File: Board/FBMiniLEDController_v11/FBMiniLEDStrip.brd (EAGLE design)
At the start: 17.8 x 82.5 mm, 20 parts, among them J4 POWER_JACKPTH_LOCK, U1 74LVC2T45

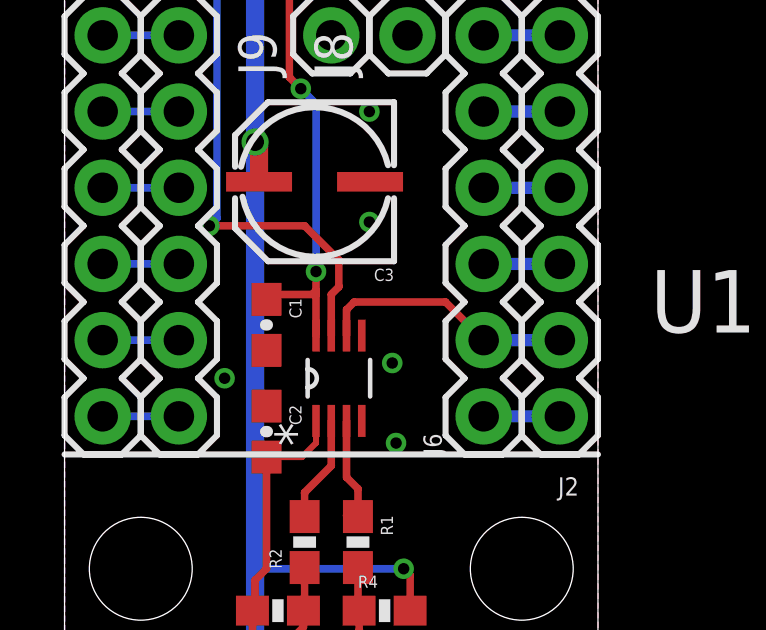
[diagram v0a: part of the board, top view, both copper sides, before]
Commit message: Updated v1.1 schematic with a lot more good information - no board changes.
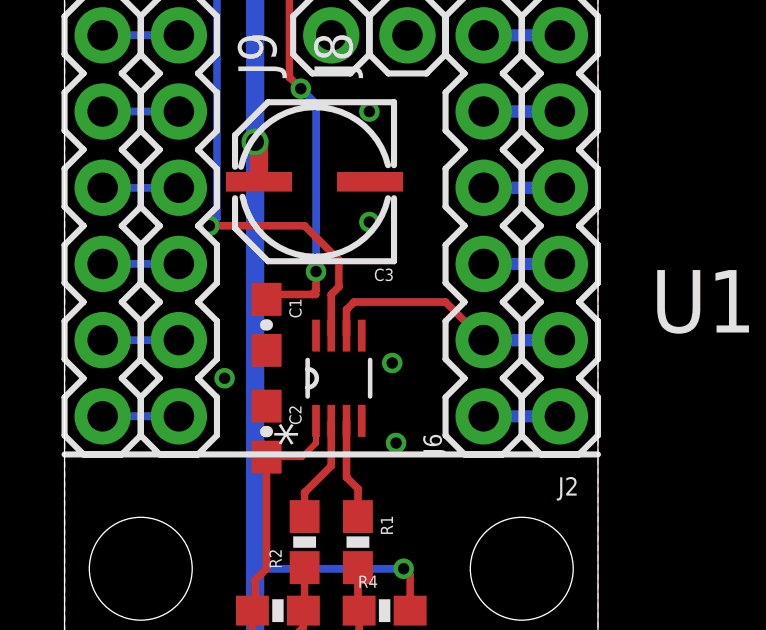
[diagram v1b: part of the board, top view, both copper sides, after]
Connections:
- net N$10 renamed 4
- net N$11 renamed 5
- net N$12 renamed 6
- net N$13 renamed 7
- net N$14 renamed 8
- net N$15 renamed 9
- net N$16 renamed 10
- net N$17 renamed 11
- net N$18 renamed 12
- net N$19 renamed 13
- net N$20 renamed 14
- net N$21 renamed 15
- net N$22 renamed 16
- net N$26 renamed N.C
- net N$27 renamed 32
- net N$28 renamed 31
- net N$29 renamed 30
- net N$30 renamed 29
- net N$31 renamed 28
- net N$32 renamed 27
- net N$33 renamed 26
- net N$34 renamed 25
- net N$35 renamed 24
- net N$36 renamed 23
- net N$37 renamed 22
- net N$38 renamed 21
- net N$39 renamed 20
- net N$40 renamed 19
- net N$41 renamed 18
- net N$42 renamed 17
- net N$9 renamed 3
- removed net N$25: C1.1, J2.18, J6.18, U1.8
- new net +3.3V: C1.1, J2.18, J6.18
- new net +3V3: U1.8
- new net 0: J1.4
- new net 1: J1.5
- new net 2: J1.6
- new net 3.3V_: J1.3
- new net VOUT: J1.1
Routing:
- net N$25: track 49.8 -> 0.00 mm, vias 2 -> 0
- net +3.3V: track 0.00 -> 48.5 mm, vias 0 -> 2
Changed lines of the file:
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@@
 </elements>
 <signals>
-<signal name="N$9">
+<signal name="3">
 <contactref element="J1" pad="7"/>
 <contactref element="J5" pad="1"/>
@@
 <wire x1="8.89" y1="29.464" x2="8.89" y2="28.0924" width="0.254" layer="1"/>
 </signal>
-<signal name="N$10">
+<signal name="4">
 <contactref element="J1" pad="8"/>
 <contactref element="J5" pad="2"/>
 <wire x1="3.81" y1="55.88" x2="1.27" y2="55.88" width="0.254" layer="16"/>
 </signal>
-<signal name="N$11">
+<signal name="5">
 <contactref element="J1" pad="9"/>
 <contactref element="J5" pad="3"/>
 <wire x1="1.27" y1="53.34" x2="3.81" y2="53.34" width="0.254" layer="16"/>
 </signal>
-<signal name="N$12">
+<signal name="6">
 <contactref element="J1" pad="10"/>
 <contactref element="J5" pad="4"/>
 <wire x1="3.81" y1="50.8" x2="1.27" y2="50.8" width="0.254" layer="16"/>
 </signal>
-<signal name="N$13">
+<signal name="7">
 <contactref element="J1" pad="11"/>
 <contactref element="J5" pad="5"/>
 <wire x1="1.27" y1="48.26" x2="3.81" y2="48.26" width="0.254" layer="16"/>
 </signal>
-<signal name="N$14">
+<signal name="8">
 <contactref element="J1" pad="12"/>
 <contactref element="J5" pad="6"/>
 <wire x1="3.81" y1="45.72" x2="1.27" y2="45.72" width="0.254" layer="16"/>
 </signal>
-<signal name="N$15">
+<signal name="9">
 <contactref element="J1" pad="13"/>
 <contactref element="J5" pad="7"/>
 <wire x1="3.81" y1="43.18" x2="1.27" y2="43.18" width="0.254" layer="16"/>
 </signal>
-<signal name="N$16">
+<signal name="10">
 <contactref element="J1" pad="14"/>
 <contactref element="J5" pad="8"/>
 <wire x1="1.27" y1="40.64" x2="3.81" y2="40.64" width="0.254" layer="16"/>
 </signal>
-<signal name="N$17">
+<signal name="11">
 <contactref element="J1" pad="15"/>
 <contactref element="J5" pad="9"/>
 <wire x1="3.81" y1="38.1" x2="1.27" y2="38.1" width="0.254" layer="16"/>
 </signal>
-<signal name="N$18">
+<signal name="12">
 <contactref element="J1" pad="16"/>
 <contactref element="J5" pad="10"/>
 <wire x1="3.81" y1="35.56" x2="1.27" y2="35.56" width="0.254" layer="16"/>
 </signal>
-<signal name="N$19">
+<signal name="13">
 <contactref element="J1" pad="17"/>
 <contactref element="J5" pad="11"/>
 <wire x1="1.27" y1="33.02" x2="3.81" y2="33.02" width="0.254" layer="16"/>
 </signal>
-<signal name="N$20">
+<signal name="14">
 <contactref element="J1" pad="18"/>
 <contactref element="J5" pad="12"/>
 <wire x1="3.81" y1="30.48" x2="1.27" y2="30.48" width="0.254" layer="16"/>
 </signal>
-<signal name="N$21">
+<signal name="15">
 <contactref element="J1" pad="19"/>
 <contactref element="J5" pad="13"/>
 <wire x1="1.27" y1="27.94" x2="3.81" y2="27.94" width="0.254" layer="16"/>
 </signal>
-<signal name="N$22">
+<signal name="16">
 <contactref element="J1" pad="20"/>
 <contactref element="J5" pad="14"/>
 <wire x1="3.81" y1="25.4" x2="1.27" y2="25.4" width="0.254" layer="16"/>
 </signal>
-<signal name="N$25">
-<contactref element="J2" pad="18"/>
-<contactref element="U1" pad="8"/>
-<contactref element="C1" pad="1"/>
-<wire x1="6.643" y1="29.21" x2="6.731" y2="29.298" width="0.2032" layer="1"/>
-<wire x1="7.874" y1="36.322" x2="7.493" y2="36.703" width="0.254" layer="1"/>
-<wire x1="7.493" y1="36.703" x2="7.493" y2="56.515" width="0.254" layer="1"/>
-<wire x1="7.493" y1="56.515" x2="8.509" y2="57.531" width="0.254" layer="1"/>
-<wire x1="8.509" y1="57.531" x2="11.684" y2="57.531" width="0.254" layer="1"/>
-<contactref element="J6" pad="18"/>
-<wire x1="13.97" y1="68.58" x2="16.51" y2="68.58" width="0.4064" layer="16"/>
-<wire x1="11.684" y1="57.531" x2="12.319" y2="58.166" width="0.254" layer="1"/>
-<wire x1="12.319" y1="58.166" x2="12.319" y2="66.929" width="0.254" layer="1"/>
-<wire x1="12.319" y1="66.929" x2="13.97" y2="68.58" width="0.254" layer="1"/>
-<wire x1="8.382" y1="29.464" x2="8.382" y2="28.0924" width="0.254" layer="1"/>
-<wire x1="8.382" y1="29.464" x2="8.255" y2="29.464" width="0.254" layer="1"/>
-<wire x1="8.255" y1="29.464" x2="6.897" y2="29.464" width="0.254" layer="1"/>
-<wire x1="6.897" y1="29.464" x2="6.731" y2="29.298" width="0.254" layer="1"/>
-<via x="7.874" y="36.322" extent="1-16" drill="0.381"/>
-<wire x1="8.382" y1="35.814" x2="7.874" y2="36.322" width="0.254" layer="16"/>
-<via x="8.382" y="30.226" extent="1-16" drill="0.381"/>
-<wire x1="8.382" y1="30.226" x2="8.382" y2="29.591" width="0.254" layer="1"/>
-<wire x1="8.382" y1="29.591" x2="8.255" y2="29.464" width="0.254" layer="1"/>
-<wire x1="8.382" y1="35.814" x2="8.382" y2="30.226" width="0.254" layer="16"/>
-</signal>
-<signal name="N$26">
+<signal name="N.C">
 <contactref element="J2" pad="17"/>
 <contactref element="J6" pad="17"/>
 <wire x1="13.97" y1="66.04" x2="16.51" y2="66.04" width="0.4064" layer="16"/>
 </signal>
-<signal name="N$27">
+<signal name="32">
 <contactref element="J2" pad="16"/>
 <contactref element="J6" pad="16"/>
 <wire x1="13.97" y1="63.5" x2="16.51" y2="63.5" width="0.4064" layer="16"/>
 </signal>
-<signal name="N$28">
+<signal name="31">
 <contactref element="J2" pad="15"/>
 <contactref element="J6" pad="15"/>
 <wire x1="13.97" y1="60.96" x2="16.51" y2="60.96" width="0.4064" layer="16"/>
 </signal>
-<signal name="N$29">
+<signal name="30">
 <contactref element="J2" pad="14"/>
 <contactref element="J6" pad="14"/>
 <wire x1="13.97" y1="58.42" x2="16.51" y2="58.42" width="0.4064" layer="16"/>
 </signal>
-<signal name="N$30">
+<signal name="29">
 <contactref element="J2" pad="13"/>
 <contactref element="J6" pad="13"/>
 <wire x1="13.97" y1="55.88" x2="16.51" y2="55.88" width="0.4064" layer="16"/>
 </signal>
-<signal name="N$31">
+<signal name="28">
 <contactref element="J2" pad="12"/>
 <contactref element="J6" pad="12"/>
 <wire x1="13.97" y1="53.34" x2="16.51" y2="53.34" width="0.4064" layer="16"/>
 </signal>
-<signal name="N$32">
+<signal name="27">
 <contactref element="J2" pad="11"/>
 <contactref element="J6" pad="11"/>
 <wire x1="13.97" y1="50.8" x2="16.51" y2="50.8" width="0.4064" layer="16"/>
 </signal>
-<signal name="N$33">
+<signal name="26">
 <contactref element="J2" pad="10"/>
 <contactref element="J6" pad="10"/>
 <wire x1="13.97" y1="48.26" x2="16.51" y2="48.26" width="0.4064" layer="16"/>
 </signal>
-<signal name="N$34">
+<signal name="25">
 <contactref element="J2" pad="9"/>
 <contactref element="J6" pad="9"/>
 <wire x1="13.97" y1="45.72" x2="16.51" y2="45.72" width="0.4064" layer="16"/>
 </signal>
-<signal name="N$35">
+<signal name="24">
 <contactref element="J2" pad="8"/>
 <contactref element="J6" pad="8"/>
 <wire x1="13.97" y1="43.18" x2="16.51" y2="43.18" width="0.4064" layer="16"/>
 </signal>
-<signal name="N$36">
+<signal name="23">
 <contactref element="J2" pad="7"/>
 <contactref element="J6" pad="7"/>
 <wire x1="13.97" y1="40.64" x2="16.51" y2="40.64" width="0.4064" layer="16"/>
 </signal>
-<signal name="N$37">
+<signal name="22">
 <contactref element="J2" pad="6"/>
 <contactref element="J6" pad="6"/>
 <wire x1="13.97" y1="38.1" x2="16.51" y2="38.1" width="0.4064" layer="16"/>
 </signal>
-<signal name="N$38">
+<signal name="21">
 <contactref element="J2" pad="5"/>
 <contactref element="J6" pad="5"/>
 <wire x1="13.97" y1="35.56" x2="16.51" y2="35.56" width="0.4064" layer="16"/>
 </signal>
-<signal name="N$39">
+<signal name="20">
 <contactref element="J2" pad="4"/>
 <contactref element="J6" pad="4"/>
 <wire x1="13.97" y1="33.02" x2="16.51" y2="33.02" width="0.4064" layer="16"/>
 </signal>
-<signal name="N$40">
+<signal name="19">
 <contactref element="J2" pad="3"/>
 <contactref element="J6" pad="3"/>
 <wire x1="13.97" y1="30.48" x2="16.51" y2="30.48" width="0.4064" layer="16"/>
 </signal>
-<signal name="N$41">
+<signal name="18">
 <contactref element="J2" pad="2"/>
 <contactref element="U1" pad="6"/>
@@
 <wire x1="9.398" y1="28.956" x2="9.398" y2="28.0924" width="0.254" layer="1"/>
 </signal>
-<signal name="N$42">
+<signal name="17">
 <contactref element="J2" pad="1"/>
 <contactref element="J6" pad="1"/>
@@
 <wire x1="8.001" y1="22.86" x2="8.001" y2="22.059" width="0.254" layer="1"/>
 </signal>
+<signal name="VOUT">
+<contactref element="J1" pad="1"/>
+</signal>
+<signal name="3.3V_">
+<contactref element="J1" pad="3"/>
+</signal>
+<signal name="0">
+<contactref element="J1" pad="4"/>
+</signal>
+<signal name="1">
+<contactref element="J1" pad="5"/>
+</signal>
+<signal name="2">
+<contactref element="J1" pad="6"/>
+</signal>
+<signal name="+3.3V">
+<contactref element="J2" pad="18"/>
+<contactref element="C1" pad="1"/>
+<contactref element="J6" pad="18"/>
+<wire x1="6.643" y1="29.21" x2="6.731" y2="29.298" width="0.2032" layer="1"/>
+<wire x1="7.874" y1="36.322" x2="7.493" y2="36.703" width="0.254" layer="1"/>
+<wire x1="7.493" y1="36.703" x2="7.493" y2="56.515" width="0.254" layer="1"/>
+<wire x1="7.493" y1="56.515" x2="8.509" y2="57.531" width="0.254" layer="1"/>
+<wire x1="8.509" y1="57.531" x2="11.684" y2="57.531" width="0.254" layer="1"/>
+<wire x1="13.97" y1="68.58" x2="16.51" y2="68.58" width="0.4064" layer="16"/>
+<wire x1="11.684" y1="57.531" x2="12.319" y2="58.166" width="0.254" layer="1"/>
+<wire x1="12.319" y1="58.166" x2="12.319" y2="66.929" width="0.254" layer="1"/>
+<wire x1="12.319" y1="66.929" x2="13.97" y2="68.58" width="0.254" layer="1"/>
+<wire x1="8.382" y1="29.464" x2="8.255" y2="29.464" width="0.254" layer="1"/>
+<wire x1="8.255" y1="29.464" x2="6.897" y2="29.464" width="0.254" layer="1"/>
+<wire x1="6.897" y1="29.464" x2="6.731" y2="29.298" width="0.254" layer="1"/>
+<via x="7.874" y="36.322" extent="1-16" drill="0.381"/>
+<wire x1="8.382" y1="35.814" x2="7.874" y2="36.322" width="0.254" layer="16"/>
+<via x="8.382" y="30.226" extent="1-16" drill="0.381"/>
+<wire x1="8.382" y1="30.226" x2="8.382" y2="29.591" width="0.254" layer="1"/>
+<wire x1="8.382" y1="29.591" x2="8.255" y2="29.464" width="0.254" layer="1"/>
+<wire x1="8.382" y1="35.814" x2="8.382" y2="30.226" width="0.254" layer="16"/>
+</signal>
+<signal name="+3V3">
+<contactref element="U1" pad="8"/>
+</signal>
 </signals>
